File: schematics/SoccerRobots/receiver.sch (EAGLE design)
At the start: 6 parts

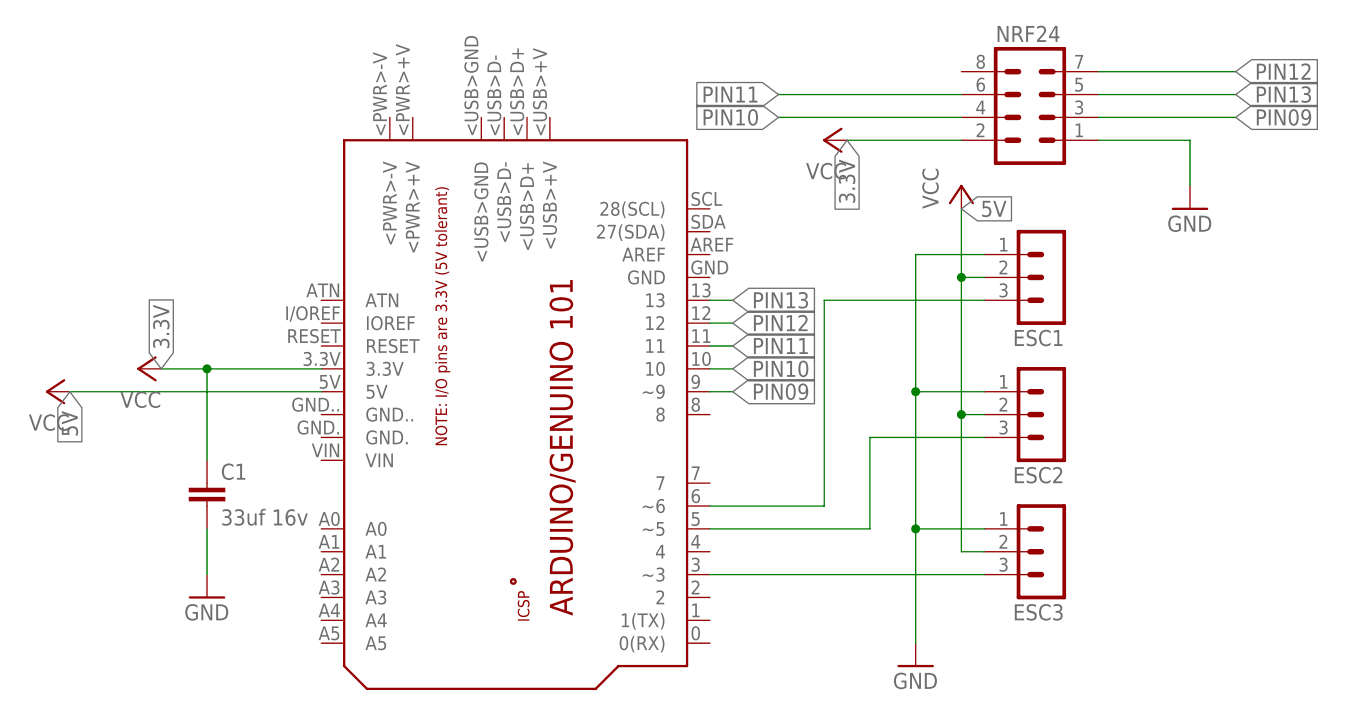
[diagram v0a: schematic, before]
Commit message: Changed receiver schematic, remember to change back
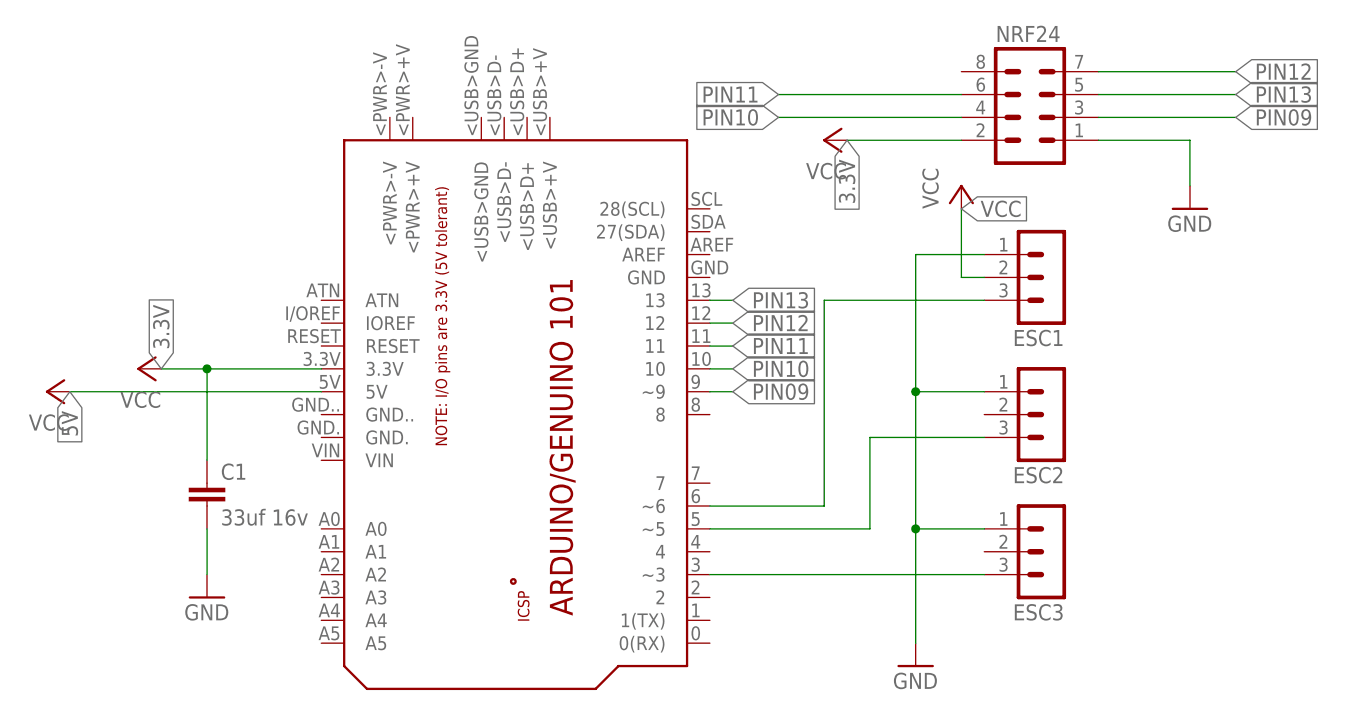
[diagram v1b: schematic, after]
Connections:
- new net VCC: ESC1.2
- net 5V: no longer ESC1.2, ESC2.2, ESC3.2
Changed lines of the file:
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@@
 <net name="5V" class="0">
-<segment>
-<pinref part="ESC1" gate="G$1" pin="2"/>
-<wire x1="101.6" y1="66.04" x2="99.06" y2="66.04" width="0.1524" layer="91"/>
-<wire x1="99.06" y1="66.04" x2="99.06" y2="50.8" width="0.1524" layer="91"/>
-<pinref part="ESC3" gate="G$1" pin="2"/>
-<wire x1="99.06" y1="50.8" x2="99.06" y2="35.56" width="0.1524" layer="91"/>
-<wire x1="99.06" y1="35.56" x2="101.6" y2="35.56" width="0.1524" layer="91"/>
-<pinref part="ESC2" gate="G$1" pin="2"/>
-<wire x1="101.6" y1="50.8" x2="99.06" y2="50.8" width="0.1524" layer="91"/>
-<junction x="99.06" y="50.8"/>
-<pinref part="5V" gate="VCC" pin="VCC"/>
-<wire x1="99.06" y1="73.66" x2="99.06" y2="66.04" width="0.1524" layer="91"/>
-<junction x="99.06" y="66.04"/>
-<label x="99.06" y="73.66" size="1.778" layer="95" xref="yes"/>
-</segment>
 <segment>
 <pinref part="PCB1" gate="G$1" pin="5V"/>
@@
 </segment>
 </net>
+<net name="VCC" class="0">
+<segment>
+<pinref part="ESC1" gate="G$1" pin="2"/>
+<wire x1="101.6" y1="66.04" x2="99.06" y2="66.04" width="0.1524" layer="91"/>
+<pinref part="5V" gate="VCC" pin="VCC"/>
+<wire x1="99.06" y1="73.66" x2="99.06" y2="66.04" width="0.1524" layer="91"/>
+<label x="99.06" y="73.66" size="1.778" layer="95" xref="yes"/>
+</segment>
+</net>
